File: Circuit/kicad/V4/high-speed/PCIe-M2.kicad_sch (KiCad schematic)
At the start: 17 parts, among them J6 Bus_M.2_Socket_M, M1 M.2 Solder Nut, M2 M.2 Solder Nut, M3 M.2 Screw, U32 AP22815AWU, U7 ASEK-32.768KHZ-L-R-T

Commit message: high speed first step
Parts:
- renumbered C8 to C12, C9 to C13, C10 to C14, CT1 to CT2, D16 to D4, J6 to J9, R15 to R12, R10 to R13, R11 to R14, TP1 to TP34, U7 to U6, U32 to U7
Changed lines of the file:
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@@
 		(dnp no)
 		(fields_autoplaced yes)
-		(property "Reference" "CT1"
+		(property "Reference" "CT2"
 			(at 179.07 146.7738 0)
 			(effects
@@
 			(project ""
 				(path "/e63e39d7-6ac0-4ffd-8aa3-1841a4541b55/00000000-0000-0000-0000-00005ed4bb5b"
-					(reference "CT1")
+					(reference "CT2")
 					(unit 1)
 				)
@@
 		(dnp no)
 		(fields_autoplaced yes)
-		(property "Reference" "C10"
+		(property "Reference" "C14"
 			(at 166.37 147.3199 0)
 			(effects
@@
 			(project ""
 				(path "/e63e39d7-6ac0-4ffd-8aa3-1841a4541b55/00000000-0000-0000-0000-00005ed4bb5b"
-					(reference "C10")
+					(reference "C14")
 					(unit 1)
 				)
@@
 		(on_board yes)
 		(dnp no)
-		(property "Reference" "#PWR035"
+		(property "Reference" "#PWR054"
 			(at 104.14 137.16 0)
 			(effects
@@
 			(project "CM5IO"
 				(path "/e63e39d7-6ac0-4ffd-8aa3-1841a4541b55/00000000-0000-0000-0000-00005ed4bb5b"
-					(reference "#PWR035")
+					(reference "#PWR054")
 					(unit 1)
 				)
@@
 		(on_board yes)
 		(dnp no)
-		(property "Reference" "R15"
+		(property "Reference" "R12"
 			(at 166.878 82.6516 0)
 			(effects
@@
 			(project "CM5IO"
 				(path "/e63e39d7-6ac0-4ffd-8aa3-1841a4541b55/00000000-0000-0000-0000-00005ed4bb5b"
-					(reference "R15")
+					(reference "R12")
 					(unit 1)
 				)
@@
 		(dnp no)
 		(fields_autoplaced yes)
-		(property "Reference" "C9"
+		(property "Reference" "C13"
 			(at 153.67 147.3199 0)
 			(effects
@@
 			(project "CM5IO"
 				(path "/e63e39d7-6ac0-4ffd-8aa3-1841a4541b55/00000000-0000-0000-0000-00005ed4bb5b"
-					(reference "C9")
+					(reference "C13")
 					(unit 1)
 				)
@@
 		(dnp no)
 		(fields_autoplaced yes)
-		(property "Reference" "U7"
+		(property "Reference" "U6"
 			(at 179.07 121.285 0)
 			(effects
@@
 			(project "CM5IO"
 				(path "/e63e39d7-6ac0-4ffd-8aa3-1841a4541b55/00000000-0000-0000-0000-00005ed4bb5b"
-					(reference "U7")
+					(reference "U6")
 					(unit 1)
 				)
@@
 		(dnp no)
 		(fields_autoplaced yes)
-		(property "Reference" "R11"
+		(property "Reference" "R14"
 			(at 54.61 168.91 90)
 			(effects
@@
 			(project "CM5IO"
 				(path "/e63e39d7-6ac0-4ffd-8aa3-1841a4541b55/00000000-0000-0000-0000-00005ed4bb5b"
-					(reference "R11")
+					(reference "R14")
 					(unit 1)
 				)
@@
 		(dnp no)
 		(fields_autoplaced yes)
-		(property "Reference" "TP1"
+		(property "Reference" "TP34"
 			(at 161.29 24.6379 0)
 			(effects
@@
 			(project "CM5IO"
 				(path "/e63e39d7-6ac0-4ffd-8aa3-1841a4541b55/00000000-0000-0000-0000-00005ed4bb5b"
-					(reference "TP1")
+					(reference "TP34")
 					(unit 1)
 				)
@@
 		(on_board yes)
 		(dnp no)
-		(property "Reference" "#PWR036"
+		(property "Reference" "#PWR057"
 			(at 176.53 161.29 0)
 			(effects
@@
 			(project "CM5IO"
 				(path "/e63e39d7-6ac0-4ffd-8aa3-1841a4541b55/00000000-0000-0000-0000-00005ed4bb5b"
-					(reference "#PWR036")
+					(reference "#PWR057")
 					(unit 1)
 				)
@@
 		(dnp no)
 		(fields_autoplaced yes)
-		(property "Reference" "D16"
+		(property "Reference" "D4"
 			(at 66.3575 156.21 0)
 			(effects
@@
 			(project "CM5IO"
 				(path "/e63e39d7-6ac0-4ffd-8aa3-1841a4541b55/00000000-0000-0000-0000-00005ed4bb5b"
-					(reference "D16")
+					(reference "D4")
 					(unit 1)
 				)
@@
 		(on_board yes)
 		(dnp no)
-		(property "Reference" "#PWR034"
+		(property "Reference" "#PWR058"
 			(at 96.52 176.53 0)
 			(effects
@@
 			(project "CM5IO"
 				(path "/e63e39d7-6ac0-4ffd-8aa3-1841a4541b55/00000000-0000-0000-0000-00005ed4bb5b"
-					(reference "#PWR034")
+					(reference "#PWR058")
 					(unit 1)
 				)
@@
 		(on_board yes)
 		(dnp no)
-		(property "Reference" "#PWR038"
+		(property "Reference" "#PWR056"
 			(at 196.85 151.13 0)
 			(effects
@@
 			(project "CM5IO"
 				(path "/e63e39d7-6ac0-4ffd-8aa3-1841a4541b55/00000000-0000-0000-0000-00005ed4bb5b"
-					(reference "#PWR038")
+					(reference "#PWR056")
 					(unit 1)
 				)
@@
 		(on_board yes)
 		(dnp no)
-		(property "Reference" "J6"
+		(property "Reference" "J9"
 			(at 101.854 33.782 0)
 			(effects
@@
 			(project "CM5IO"
 				(path "/e63e39d7-6ac0-4ffd-8aa3-1841a4541b55/00000000-0000-0000-0000-00005ed4bb5b"
-					(reference "J6")
+					(reference "J9")
 					(unit 1)
 				)
@@
 		(dnp no)
 		(fields_autoplaced yes)
-		(property "Reference" "R10"
+		(property "Reference" "R13"
 			(at 74.93 154.9399 0)
 			(effects
@@
 			(project "CM5IO"
 				(path "/e63e39d7-6ac0-4ffd-8aa3-1841a4541b55/00000000-0000-0000-0000-00005ed4bb5b"
-					(reference "R10")
+					(reference "R13")
 					(unit 1)
 				)
@@
 		(dnp no)
 		(fields_autoplaced yes)
-		(property "Reference" "U32"
+		(property "Reference" "U7"
 			(at 96.52 149.86 0)
 			(effects
@@
 			(project ""
 				(path "/e63e39d7-6ac0-4ffd-8aa3-1841a4541b55/00000000-0000-0000-0000-00005ed4bb5b"
-					(reference "U32")
+					(reference "U7")
 					(unit 1)
 				)
@@
 		(on_board yes)
 		(dnp no)
-		(property "Reference" "#PWR037"
+		(property "Reference" "#PWR055"
 			(at 166.37 143.51 0)
 			(effects
@@
 			(project "CM5IO"
 				(path "/e63e39d7-6ac0-4ffd-8aa3-1841a4541b55/00000000-0000-0000-0000-00005ed4bb5b"
-					(reference "#PWR037")
+					(reference "#PWR055")
 					(unit 1)
 				)
@@
 		(dnp no)
 		(fields_autoplaced yes)
-		(property "Reference" "C8"
+		(property "Reference" "C12"
 			(at 142.24 147.3199 0)
 			(effects
@@
 			(project "CM5IO"
 				(path "/e63e39d7-6ac0-4ffd-8aa3-1841a4541b55/00000000-0000-0000-0000-00005ed4bb5b"
-					(reference "C8")
+					(reference "C12")
 					(unit 1)
 				)

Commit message: kicad: high speed V2.2 Circuit finish psu bom update
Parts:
- removed C12, C13, C14: 1uf, Capacitor_SMD:C_0805_2012Metric, symbol Device:C
- removed CT2: 100uf, Capacitor_Tantalum_SMD:CP_EIA-7343-31_Kemet-D, symbol Device:C_Polarized_Small
- added C17: 1uf, Capacitor_SMD:C_0805_2012Metric, symbol Device:C
- added C18: 100nf, Capacitor_SMD:C_0805_2012Metric, symbol Device:C
- added C20: 22nf c0g, Capacitor_SMD:C_0805_2012Metric, symbol Device:C
- added CT3, CT4: 100uF, Capacitor_Tantalum_SMD:CP_EIA-7343-31_Kemet-D, symbol Device:C_Polarized_Small
- C19: renamed from C11; value 100n -> 100nf; Cikkszám (none) -> 100.011.22; Field4 Farnell -> (none); Field5 2611911 -> (none); Field6 RM EMK105 B7104KV-F -> (none); Field7 TAIYO YUDEN EUROPE GMBH -> (none); Field8 110091611 -> (none); Link (none) -> https://www.hestore.hu/prod_10001122.html; Part Description 0.1uF 10% 16V Ceramic Capacitor X7R 0402 (1005 Metric) -> (none)
- D3: renamed from D4; Cikkszám (none) -> 100.365.89; Link (none) -> https://www.hestore.hu/prod_10048914.html
- D4: renamed from D3; value LED Green -> LED; Cikkszám (none) -> 100.365.89; Field4 Digikey -> (none); Field5 LTST-S270KGKT -> (none); Field6 SML-A12M8TT86N -> (none); Field7 Rohm -> (none); Field8 650263301 -> (none); Link (none) -> https://www.hestore.hu/prod_10048914.html; Part Description Green 572nm LED Indication - Discrete 2.2V 2-SMD, No Lead -> (none)
- J10: renamed from J9; footprint psu:M.2 M Key socket -> panel:M.2 M Key socket; Cikkszám (none) -> 523-MDT420M03001; Field5 MTSSD03-67MSW337 -> (none); Field6 MTSSD03-67MSW337 -> (none); Field7 MTCONN -> (none); Link (none) -> https://hu.mouser.com/ProductDetail/Amphenol-FCI/MDT420M030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; Part Description M.2 M Key connector -> (none)
- M1: renamed from M3; Cikkszám (none) -> -; Link (none) -> -; Part Description M.2 Screw -> (none); now left out of the parts list
- M2: renamed from M1; Cikkszám (none) -> -; Link (none) -> -; Part Description Solder nut for M.2 slot -> (none); now left out of the parts list
- M3: renamed from M2; Cikkszám (none) -> -; Link (none) -> -; Part Description Solder nut for M.2 slot -> (none); now left out of the parts list
- R23: renamed from R13; value 10k -> 10K; Cikkszám (none) -> 100.011.45; Link (none) -> https://www.hestore.hu/prod_10001145.html
- R24: renamed from R14; value 100 -> 100R; Cikkszám (none) -> 100.011.42; Link (none) -> https://www.hestore.hu/prod_10001142.html
- R25: renamed from R12; value 1k -> 1K; Cikkszám (none) -> 100.011.57; Field4 Farnell -> (none); Field5 9239235 -> (none); Field6 RK73H1ETTP1001F -> (none); Field7 KOA EUROPE GMBH -> (none); Field8 125049511 -> (none); Link (none) -> https://www.hestore.hu/prod_10001157.html; Part Description Resistor 1K M1005 1% 63mW -> (none)
- TP7: renamed from TP34; Cikkszám (none) -> -; Link (none) -> -; now left out of the parts list
- U6: renamed from U7; Cikkszám (none) -> 100.491.23; Link (none) -> https://www.hestore.hu/prod_10049123.html
- U7: renamed from U6; Cikkszám (none) -> 100.491.02; Field5 ASEK-32.768KHZ-L-R-T -> (none); Field6 ASEK-32.768KHZ-L-R-T -> (none); Field7 abracon -> (none); Link (none) -> https://www.hestore.hu/prod_10049102.html; Part Description 32KHz Xtal oscilator -> (none)
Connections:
- net GND: now also C17.2, C18.2, C20.2, CT3.2, CT4.2
- net M2_3v3: now also C17.1, C18.1, C20.1, CT3.1, CT4.1
- net 32.768KHZ: now reaches J10.68 (SUSCLK), U7.3 (Out)
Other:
- moved on the sheet: C19, D3, D4, J10, M1, M2, M3, R23, R24, R25, TP7, U6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

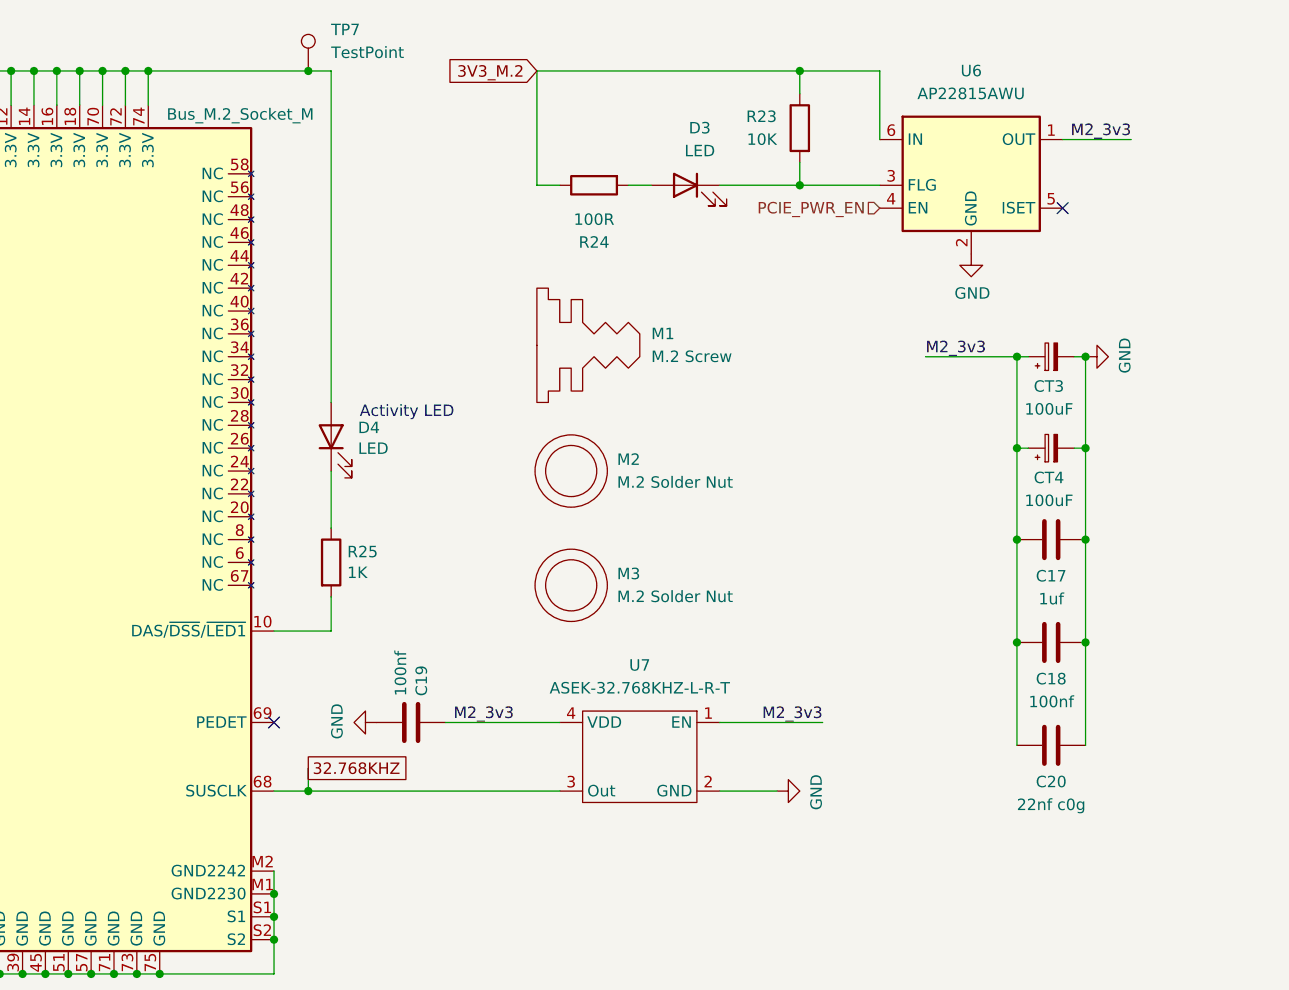
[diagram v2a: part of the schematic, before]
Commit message: finished high-speed panel schematic and first try to doute gpios
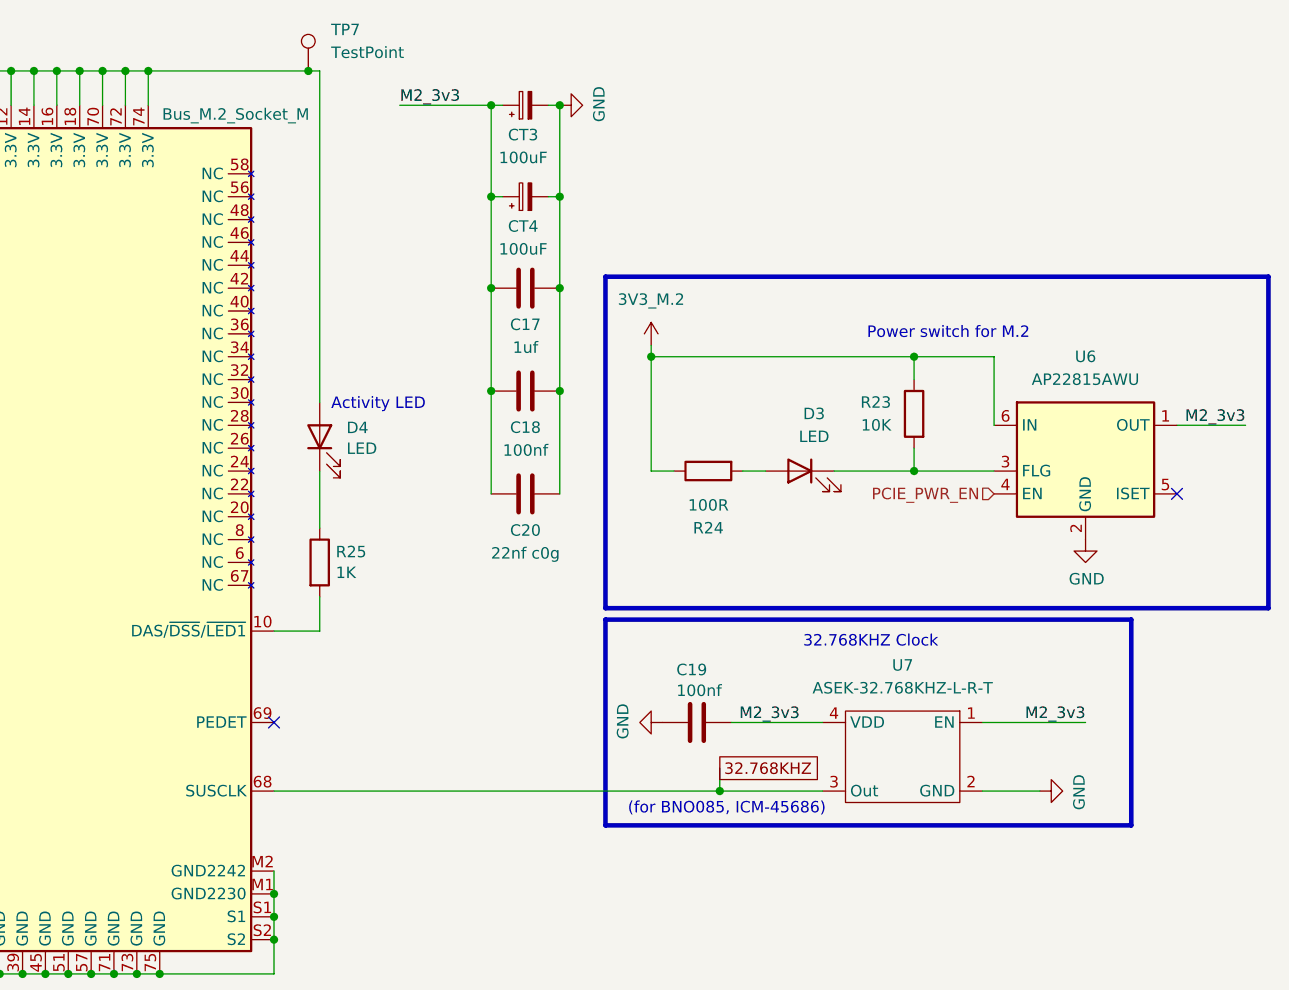
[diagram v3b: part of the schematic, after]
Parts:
- removed M1: M.2 Screw, symbol CM5IO:M.2_Screw
- removed M2, M3: M.2 Solder Nut, symbol CM5IO:SolderNut
- CT3, CT4: footprint Capacitor_Tantalum_SMD:CP_EIA-7343-31_Kemet-D -> Capacitor_Tantalum_SMD:CP_EIA-3528-21_Kemet-B
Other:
- note added: "(for BNO085, ICM-45686)"
- note added: "32.768KHZ Clock"
- note added: "Power switch for M.2"
- moved on the sheet: C17, C18, C19, C20, CT3, CT4, D3, D4, R23, R24, R25, U6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
